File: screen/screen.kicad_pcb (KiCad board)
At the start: 2 copper layers, 37 parts, among them P1 CONN_01X08, Q1 MOS_N, Q2 MOS_N, U1 uHDMI, U3 TPS76333

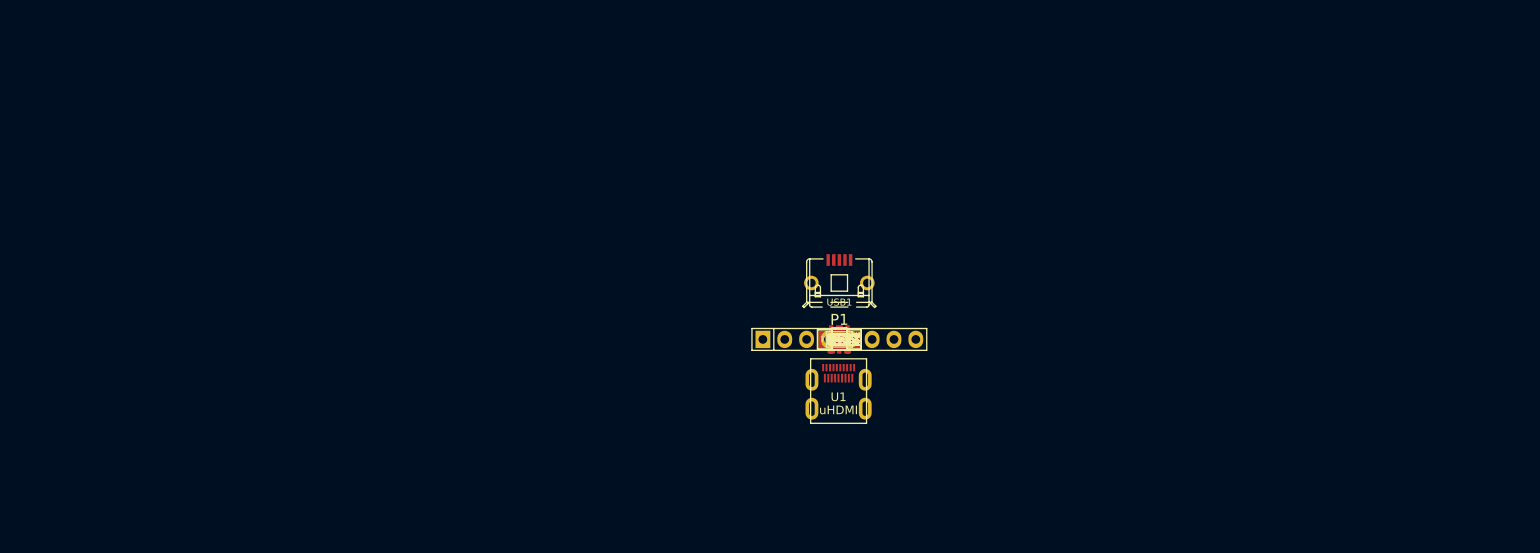
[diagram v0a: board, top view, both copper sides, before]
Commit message: finished component modules and started screen board design
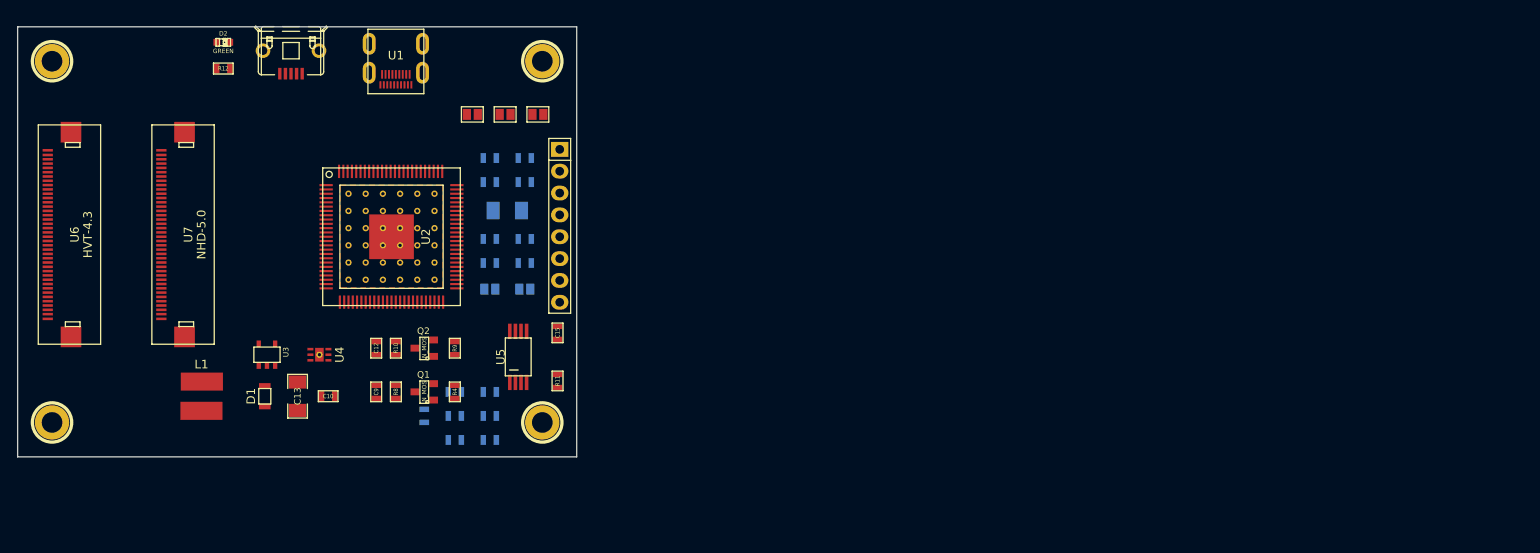
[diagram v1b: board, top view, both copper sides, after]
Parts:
- added 1PIN: P***, Connect:1pin, F.Cu at (57.1, 62.9)
- added 2PIN: P***, Connect:1pin, F.Cu at (114.1, 62.9)
- added 3PIN: P***, Connect:1pin, F.Cu at (57.1, 104.9)
- added 4PIN: P***, Connect:1pin, F.Cu at (114.1, 104.9)
- added D1: DIODESCH, SCREEN:SOD323, F.Cu at (81.8, 101.9)
- added D2: GREEN, LEDs:LED-0603, F.Cu at (77.0, 60.7)
- added L1: 22uH, SCREEN:VLCF5020, F.Cu at (74.4, 101.9)
- added R12: 510R, SMD_Packages:SMD-0603, F.Cu at (77.0, 63.8)
- added U2: TFP401A, SCREEN:TFP401A, F.Cu at (96.5, 83.3)
- added U4: TSP61161, SCREEN:TSP61161, F.Cu at (88.1, 97.0)
- added U5: M93C46, SCREEN:TSSOP8, F.Cu at (111.3, 97.3)
- added U6: HVT-4.3, SCREEN:40_PIN, F.Cu at (60.5, 83.1)
- added U7: NHD-5.0, SCREEN:40_PIN, F.Cu at (73.7, 83.1)
- C1, C11, C14, C2, C3, C4, C5, C6, C7, C8, JP4, JP5, R1, R2, R3, R5, R6, R7: moved to B.Cu
- Q1, Q2: value MOS_N -> N_MOS
- moved USB1 71.6 mm to (84.8, 58.9), turned to 180 degrees
- moved U1 68.9 mm to (97.0, 59.2), turned to 180 degrees
- moved U3 66.6 mm to (82.0, 97.0)
- moved C13 63.3 mm to (85.6, 101.9), turned to 270 degrees
- moved C10 59.8 mm to (89.2, 101.9)
- moved C9 54.2 mm to (94.7, 101.3), turned to 90 degrees
- moved C12 53.9 mm to (94.7, 96.3), turned to 270 degrees
- moved R8 51.9 mm to (97.0, 101.3), turned to 270 degrees
- moved R10 51.6 mm to (97.0, 96.3), turned to 90 degrees
- moved JP1 50.1 mm to (105.9, 69.1), turned to 90 degrees
- moved R3 49.1 mm to (100.3, 104.1), turned to 90 degrees
- moved Q1 48.6 mm to (100.3, 101.3), turned to 90 degrees
- moved Q2 48.3 mm to (100.3, 96.3), turned to 90 degrees
- moved JP2 46.8 mm to (109.7, 69.1), turned to 270 degrees
- moved C7 46.2 mm to (103.9, 106.9), turned to 180 degrees
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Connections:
- Q1 pad 1: (no net) -> A_ON
- Q1 pad 2: (no net) -> GND
- Q1 pad 3: (no net) -> AVDD
- Q2 pad 1: (no net) -> V_ON
- Q2 pad 2: (no net) -> GND
- Q2 pad 3: (no net) -> VDD
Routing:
- added copper zone on F.Cu, net GND
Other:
- board outline added: 65 x 50 mm
- net class Default: clearance 0.254 -> 0.1524; trace_width 0.254 -> 0.1524; via_dia 0.889 -> 0.7366; via_drill 0.635 -> 0.381
- rule trace_clearance: 0.254 -> 0.1524
- rule trace_min: 0.254 -> 0.1524
- rule via_min_drill: 0.508 -> 0.381
- rule via_min_size: 0.889 -> 0.7366

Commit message: moving around some stuff for routing
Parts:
- C10, C13, C15, D1, R11, U3, U4, U5: moved to B.Cu
- JP4, JP5, R3: moved to F.Cu
- moved U4 127.8 mm to (214.9, 80.8)
- moved D1 124.3 mm to (203.5, 76.5), turned to 0 degrees
- moved C13 121.4 mm to (203.5, 72.9), turned to 180 degrees
- moved L1 119.1 mm to (190.2, 74.2), turned to 90 degrees
- moved C10 116.4 mm to (203.5, 79.8), turned to 180 degrees
- moved U1 116.3 mm to (213.4, 58.9)
- moved 3PIN 115.3 mm to (172.0, 114.0)
- moved 1PIN 115.0 mm to (172.0, 62.0)
- moved R3 114.4 mm to (206.8, 62.2), turned to 270 degrees
- moved R12 113.0 mm to (190.0, 62.7)
- moved D2 113.0 mm to (189.9, 59.7)
- moved R11 112.9 mm to (224.5, 69.6), turned to 270 degrees
- moved U2 112.9 mm to (207.8, 102.3), turned to 180 degrees
- moved U5 112.6 mm to (221.0, 71.9), turned to 270 degrees
- moved R1 112.4 mm to (215.1, 85.1), turned to 180 degrees
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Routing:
- removed copper zone on F.Cu, net GND
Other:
- board size 65 x 50 mm -> 60 x 60 mm

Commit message: screen board is complete
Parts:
- added G1: LOGO, SCREEN:OSLOGO, F.Cu at (177.8, 114.8)
- added G2: LOGO, SCREEN:LOGO, F.Cu at (207.8, 91.4)
- R3: moved to B.Cu
- moved R3 21.9 mm to (214.1, 82.8), turned to 180 degrees
- moved R11 19.3 mm to (214.1, 85.9)
- moved C15 18.7 mm to (214.1, 89.2), turned to 90 degrees
- moved U5 15.1 mm to (209.6, 81.8)
- moved U4 11.0 mm to (209.6, 90.4)
- moved USB1 10.1 mm to (197.0, 68.0)
- moved 1PIN 10.0 mm to (172.0, 72.0)
- moved 2PIN 10.0 mm to (224.0, 72.0)
- moved D2 9.89 mm to (190.0, 69.6)
- moved JP1 9.58 mm to (177.5, 70.2)
- moved JP2 9.58 mm to (181.3, 70.2)
- moved JP3 9.58 mm to (185.1, 70.2)
- moved JP4 9.58 mm to (179.4, 74.2)
- moved JP5 9.58 mm to (183.4, 74.2)
- moved C9 9.40 mm to (190.0, 74.7)
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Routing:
- net GND: track 0.00 -> 406.9 mm, vias 0 -> 3
- net 3.3V: track 0.00 -> 168.8 mm, vias 0 -> 2
- net LED-: track 0.00 -> 92.3 mm, vias 0 -> 1
- net VBUS: track 0.00 -> 87.0 mm, vias 0 -> 1
- net LED+: track 0.00 -> 69.3 mm, vias 0 -> 1
- net DISP: track 0.00 -> 59.0 mm, vias 0 -> 2
- net ST: track 0.00 -> 55.4 mm
- net RX2-: track 0.00 -> 51.4 mm, vias 0 -> 2
- net RX1+: track 0.00 -> 51.3 mm
- net RX1-: track 0.00 -> 49.6 mm
- net RX0-: track 0.00 -> 47.6 mm, vias 0 -> 2
- net RX2+: track 0.00 -> 46.7 mm, vias 0 -> 2
- net RXC+: track 0.00 -> 44.4 mm, vias 0 -> 2
- net RXC-: track 0.00 -> 42.6 mm, vias 0 -> 2
- net RX0+: track 0.00 -> 40.6 mm
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- added copper zone on B.Cu, net GND
- added copper zone on F.Cu, net GND
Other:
- board size 60 x 60 mm -> 60 x 50 mm
- rule pad_to_mask_clearance: 0 -> 0.0508
- board text added: "5.0"
- board text added: "AON"
- board text added: "BD"
- board text added: "CTRL"
- board text added: "DISP"
- board text added: "HVT"
- board text added: "NHD"
- board text added: "PD"
- board text added: "PORTAL"
- board text added: "RST"
- board text added: "SCL"
- board text added: "SDA"
- board text added: "ST+"
- board text added: "ST-"
- board text added: "VON"
